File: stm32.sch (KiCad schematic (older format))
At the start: 30 parts, among them U3 STM32F205RBTx, U4 OLED_0.96\"_SSD1306, Y2 Crystal_GND24

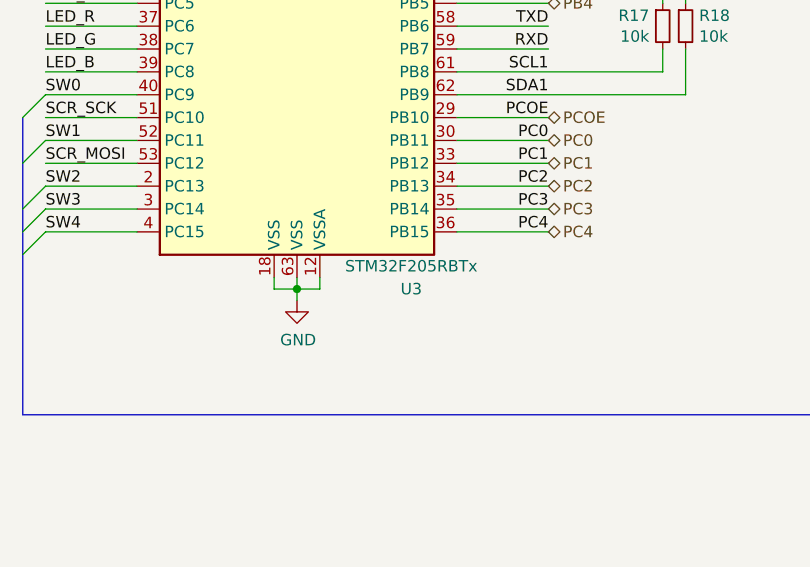
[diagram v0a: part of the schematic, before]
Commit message: sch, pcb: Replace STM32F205 with STM32F405
A Rust HAL is available for the F4 series and not for the F2 series...
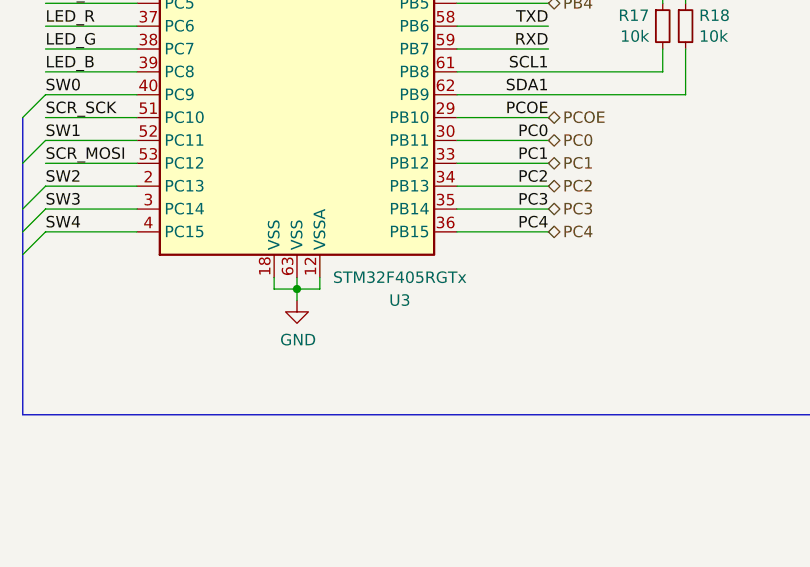
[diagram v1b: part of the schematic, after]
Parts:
- removed U3: STM32F205RBTx, Package_QFP:LQFP-64_10x10mm_P0.5mm, symbol MCU_ST_STM32F2:STM32F205RBTx
- added U3: STM32F405RGTx, Package_QFP:LQFP-64_10x10mm_P0.5mm, symbol MCU_ST_STM32F4:STM32F405RGTx
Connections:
- net +3V3: now also U3.1 (VBAT), U3.13 (VDDA), U3.19 (VDD), U3.32 (VDD), U3.48 (VDD), U3.64 (VDD)
- net DRDY: now also U3.50 (PA15)
- net GND: now also U3.12 (VSSA), U3.18 (VSS), U3.63 (VSS)
- net LED_A0: now also U3.54 (PD2)
- net LED_A1: now also U3.8 (PC0)
- net LED_A2: now also U3.9 (PC1)
- net LED_A3: now also U3.10 (PC2)
- net LED_A4: now also U3.11 (PC3)
- net LED_B: now also U3.39 (PC8)
- net LED_G: now also U3.38 (PC7)
- net LED_R: now also U3.37 (PC6)
- net PA0: now also U3.15 (PA1)
- net PA1: now also U3.16 (PA2)
- net PA2: now also U3.17 (PA3)
- net PA3: now also U3.20 (PA4)
- net PA4: now also U3.21 (PA5)
- net PA5: now also U3.22 (PA6)
- net PA6: now also U3.23 (PA7)
- net PA7: now also U3.41 (PA8)
- net PA8: now also U3.42 (PA9)
- net PA9: now also U3.43 (PA10)
- net PAOE: now also U3.14 (PA0)
- net PB0: now also U3.27 (PB1)
- net PB1: now also U3.28 (PB2)
- net PB2: now also U3.55 (PB3)
- net PB3: now also U3.56 (PB4)
- net PB4: now also U3.57 (PB5)
- net PBOE: now also U3.26 (PB0)
- net PC0: now also U3.30 (PB11)
- net PC1: now also U3.33 (PB12)
- net PC2: now also U3.34 (PB13)
- net PC3: now also U3.35 (PB14)
- net PC4: now also U3.36 (PB15)
- net PCOE: now also U3.29 (PB10)
- net RXD: now also U3.59 (PB7)
- net SCK_~CS: now also U3.25 (PC5)
- net SCL: now also U3.61 (PB8)
- net SCR_D~C: now also U3.24 (PC4)
- net SCR_MOSI: now also U3.53 (PC12)
- net SCR_SCK: now also U3.51 (PC10)
- net SDA: now also U3.62 (PB9)
- net SW0: now also U3.40 (PC9)
- net SW1: now also U3.52 (PC11)
- net SW2: now also U3.2 (PC13)
- net SW3: now also U3.3 (PC14)
- net SW4: now also U3.4 (PC15)
- net SWCLK: now also U3.49 (PA14)
- net SWDIO: now also U3.46 (PA13)
- net SWRST: now also U3.7 (NRST)
- net TXD: now also U3.58 (PB6)
- net USB_N: now also U3.44 (PA11)
- net USB_P: now also U3.45 (PA12)
- net at C19.1, Y2.1: now also U3.5 (PH0)
- net at C20.1, Y2.3: now also U3.6 (PH1)
- net at R12.2: now also U3.60 (BOOT0)
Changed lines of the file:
@@
 $EndDescr
-$Comp
-L MCU_ST_STM32F2:STM32F205RBTx U3
-U 1 1 5DFC281B
-P 5700 4050
-F 0 "U3" H 6200 2200 50  0000 C CNN
-F 1 "STM32F205RBTx" H 6200 2300 50  0000 C CNN
-F 2 "Package_QFP:LQFP-64_10x10mm_P0.5mm" H 5100 2350 50  0001 R CNN
-F 3 "http://www.st.com/st-web-ui/static/active/en/resource/technical/document/datasheet/CD00237391.pdf" H 5700 4050 50  0001 C CNN
-	1    5700 4050
-	1    0    0    -1
-$EndComp
 $Comp
 L power:+3V3 #PWR0124
@@
 Wire Wire Line
 	3900 3350 3900 3400
+Text Notes 5900 7550 0    50   ~ 0
+Red: 8mA@1.73V\nGreen: 5mA@2.7V\nBlue: 3mA@2.49V
 Wire Bus Line
 	4400 4050 4400 6450
@@
 Wire Bus Line
 	8300 5250 8300 6450
-Text Notes 5900 7550 0    50   ~ 0
-Red: 8mA@1.73V\nGreen: 5mA@2.7V\nBlue: 3mA@2.49V
+$Comp
+L MCU_ST_STM32F4:STM32F405RGTx U3
+U 1 1 5EFAF3AD
+P 5700 4050
+F 0 "U3" H 6150 2150 50  0000 C CNN
+F 1 "STM32F405RGTx" H 6150 2250 50  0000 C CNN
+F 2 "Package_QFP:LQFP-64_10x10mm_P0.5mm" H 5100 2350 50  0001 R CNN
+F 3 "http://www.st.com/st-web-ui/static/active/en/resource/technical/document/datasheet/DM00037051.pdf" H 5700 4050 50  0001 C CNN
+	1    5700 4050
+	1    0    0    -1
+$EndComp
 $EndSCHEMATC

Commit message: sch: List LCSC P/N for each component
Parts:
- C12, C13, C14, C15, C16, C17, C18, C19, C20, C21: LCSC P/N (none) -> C1591; MFR P/N (none) -> CL10B104KB8NNNC
- D3, D4, D5, D6, D7: LCSC P/N (none) -> C404281; MFR P/N (none) -> MHPA1515RGBDT
- R11, R13: LCSC P/N (none) -> C327826; MFR P/N (none) -> MR06X1003FTL
- R12, R17, R18: LCSC P/N (none) -> C115324; MFR P/N (none) -> RS-03K1002FT
- R14: LCSC P/N (none) -> C429538; MFR P/N (none) -> CR0603F196RP05
- R15: LCSC P/N (none) -> C22787; MFR P/N (none) -> 0603WAF1200T5E
- R16: LCSC P/N (none) -> C286581; MFR P/N (none) -> RS-03K2700FT
- S1: LCSC P/N (none) -> C145899; MFR P/N (none) -> K1-5202UA-03
- U3: LCSC P/N (none) -> C15742; MFR P/N (none) -> STM32F405RGT6
- U4: LCSC P/N (none) -> C358721; MFR P/N (none) -> MTF185-107SY1
- Y2: LCSC P/N (none) -> C400090; MFR P/N (none) -> TAXM8M4RDBCCT2T
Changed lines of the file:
@@
 F 2 "Resistor_SMD:R_0603_1608Metric" H 4400 2300 50  0001 C CNN
 F 3 "~" H 4400 2300 50  0001 C CNN
+F 4 "C327826" H 4400 2300 50  0001 C CNN "LCSC P/N"
+F 5 "MR06X1003FTL" H 4400 2300 50  0001 C CNN "MFR P/N"
 	1    4400 2300
 	1    0    0    -1
@@
 F 2 "Capacitor_SMD:C_0603_1608Metric" H 4400 2600 50  0001 C CNN
 F 3 "~" H 4400 2600 50  0001 C CNN
+F 4 "C1591" H 4400 2600 50  0001 C CNN "LCSC P/N"
+F 5 "CL10B104KB8NNNC" H 4400 2600 50  0001 C CNN "MFR P/N"
 	1    4400 2600
 	1    0    0    1
@@
 F 2 "Resistor_SMD:R_0603_1608Metric" H 4800 2650 50  0001 C CNN
 F 3 "~" H 4800 2650 50  0001 C CNN
+F 4 "C115324" H 4800 2650 50  0001 C CNN "LCSC P/N"
+F 5 "RS-03K1002FT" H 4800 2650 50  0001 C CNN "MFR P/N"
 	1    4800 2650
 	0    -1   1    0
@@
 F 2 "Capacitor_SMD:C_0603_1608Metric" H 4750 1300 50  0001 C CNN
 F 3 "~" H 4750 1300 50  0001 C CNN
+F 4 "C1591" H 4750 1300 50  0001 C CNN "LCSC P/N"
+F 5 "CL10B104KB8NNNC" H 4750 1300 50  0001 C CNN "MFR P/N"
 	1    4750 1300
 	-1   0    0    -1
@@
 F 2 "Capacitor_SMD:C_0603_1608Metric" H 5150 1300 50  0001 C CNN
 F 3 "~" H 5150 1300 50  0001 C CNN
+F 4 "C1591" H 5150 1300 50  0001 C CNN "LCSC P/N"
+F 5 "CL10B104KB8NNNC" H 5150 1300 50  0001 C CNN "MFR P/N"
 	1    5150 1300
 	-1   0    0    -1
@@
 F 2 "Capacitor_SMD:C_0603_1608Metric" H 5550 1300 50  0001 C CNN
 F 3 "~" H 5550 1300 50  0001 C CNN
+F 4 "C1591" H 5550 1300 50  0001 C CNN "LCSC P/N"
+F 5 "CL10B104KB8NNNC" H 5550 1300 50  0001 C CNN "MFR P/N"
 	1    5550 1300
 	-1   0    0    -1
@@
 F 2 "Capacitor_SMD:C_0603_1608Metric" H 5950 1300 50  0001 C CNN
 F 3 "~" H 5950 1300 50  0001 C CNN
+F 4 "C1591" H 5950 1300 50  0001 C CNN "LCSC P/N"
+F 5 "CL10B104KB8NNNC" H 5950 1300 50  0001 C CNN "MFR P/N"
 	1    5950 1300
 	-1   0    0    -1
@@
 F 2 "Capacitor_SMD:C_0603_1608Metric" H 6350 1300 50  0001 C CNN
 F 3 "~" H 6350 1300 50  0001 C CNN
+F 4 "C1591" H 6350 1300 50  0001 C CNN "LCSC P/N"
+F 5 "CL10B104KB8NNNC" H 6350 1300 50  0001 C CNN "MFR P/N"
 	1    6350 1300
 	-1   0    0    -1
@@
 F 2 "Capacitor_SMD:C_0603_1608Metric" H 6750 1300 50  0001 C CNN
 F 3 "~" H 6750 1300 50  0001 C CNN
+F 4 "C1591" H 6750 1300 50  0001 C CNN "LCSC P/N"
+F 5 "CL10B104KB8NNNC" H 6750 1300 50  0001 C CNN "MFR P/N"
 	1    6750 1300
 	-1   0    0    -1
@@
 F 2 "Resistor_SMD:R_0603_1608Metric" H 7300 4750 50  0001 C CNN
 F 3 "~" H 7300 4750 50  0001 C CNN
+F 4 "C115324" H 7300 4750 50  0001 C CNN "LCSC P/N"
+F 5 "RS-03K1002FT" H 7300 4750 50  0001 C CNN "MFR P/N"
 	1    7300 4750
 	1    0    0    -1
@@
 F 2 "Resistor_SMD:R_0603_1608Metric" H 7400 4750 50  0001 C CNN
 F 3 "~" H 7400 4750 50  0001 C CNN
+F 4 "C115324" H 7400 4750 50  0001 C CNN "LCSC P/N"
+F 5 "RS-03K1002FT" H 7400 4750 50  0001 C CNN "MFR P/N"
 	1    7400 4750
 	1    0    0    -1
@@
 F 2 "antboard:K1-5202UA-03" H 8900 5050 50  0001 C CNN
 F 3 "https://datasheet.lcsc.com/szlcsc/1809211421_Korean-Hroparts-Elec-K1-5202UA-03_C145899.pdf" H 8900 5050 50  0001 C CNN
+F 4 "C145899" H 8900 5050 50  0001 C CNN "LCSC P/N"
+F 5 "K1-5202UA-03" H 8900 5050 50  0001 C CNN "MFR P/N"
 	1    8900 5050
 	1    0    0    -1
@@
 F 2 "Resistor_SMD:R_0603_1608Metric" H 5250 7350 50  0001 C CNN
 F 3 "~" H 5250 7350 50  0001 C CNN
+F 4 "C429538" H 5250 7350 50  0001 C CNN "LCSC P/N"
+F 5 "CR0603F196RP05" H 5250 7350 50  0001 C CNN "MFR P/N"
 	1    5250 7350
 	0    -1   1    0
@@
 F 2 "Resistor_SMD:R_0603_1608Metric" H 5250 7450 50  0001 C CNN
 F 3 "~" H 5250 7450 50  0001 C CNN
+F 4 "C22787" H 5250 7450 50  0001 C CNN "LCSC P/N"
+F 5 "0603WAF1200T5E" H 5250 7450 50  0001 C CNN "MFR P/N"
 	1    5250 7450
 	0    -1   1    0
@@
 F 2 "Resistor_SMD:R_0603_1608Metric" H 5250 7550 50  0001 C CNN
 F 3 "~" H 5250 7550 50  0001 C CNN
+F 4 "C286581" H 5250 7550 50  0001 C CNN "LCSC P/N"
+F 5 "RS-03K2700FT" H 5250 7550 50  0001 C CNN "MFR P/N"
 	1    5250 7550
 	0    -1   1    0
@@
 F 2 "antboard:OLED_0.96_SSD1306" H 1300 4700 50  0001 C CNN
 F 3 "https://datasheet.lcsc.com/szlcsc/1809201020_Jixin-JX04010101_C131691.pdf" H 1300 4700 50  0001 C CNN
+F 4 "C358721" H 2150 4700 50  0001 C CNN "LCSC P/N"
+F 5 "MTF185-107SY1" H 2150 4700 50  0001 C CNN "MFR P/N"
 	1    2150 4700
 	-1   0    0    -1
@@
 F 2 "Capacitor_SMD:C_0603_1608Metric" H 2800 5250 50  0001 C CNN
 F 3 "~" H 2800 5250 50  0001 C CNN
+F 4 "C1591" H 2800 5250 50  0001 C CNN "LCSC P/N"
+F 5 "CL10B104KB8NNNC" H 2800 5250 50  0001 C CNN "MFR P/N"
 	1    2800 5250
 	-1   0    0    1
@@
 F 2 "Resistor_SMD:R_0603_1608Metric" H 2800 4750 50  0001 C CNN
 F 3 "~" H 2800 4750 50  0001 C CNN
+F 4 "C327826" H 2800 4750 50  0001 C CNN "LCSC P/N"
+F 5 "MR06X1003FTL" H 2800 4750 50  0001 C CNN "MFR P/N"
 	1    2800 4750
 	1    0    0    -1
@@
 F 2 "antboard:PLCC1515" H 1000 7000 50  0001 C CNN
 F 3 "~" H 1000 7000 50  0001 C CNN
+F 4 "C404281" H 1000 7050 50  0001 C CNN "LCSC P/N"
+F 5 "MHPA1515RGBDT" H 1000 7050 50  0001 C CNN "MFR P/N"
 	1    1000 7050
 	0    -1   -1   0
@@
 F 2 "antboard:PLCC1515" H 1750 7000 50  0001 C CNN
 F 3 "~" H 1750 7000 50  0001 C CNN
+F 4 "C404281" H 1750 7050 50  0001 C CNN "LCSC P/N"
+F 5 "MHPA1515RGBDT" H 1750 7050 50  0001 C CNN "MFR P/N"
 	1    1750 7050
 	0    -1   -1   0
@@
 F 2 "antboard:PLCC1515" H 2500 7000 50  0001 C CNN
 F 3 "~" H 2500 7000 50  0001 C CNN
+F 4 "C404281" H 2500 7050 50  0001 C CNN "LCSC P/N"
+F 5 "MHPA1515RGBDT" H 2500 7050 50  0001 C CNN "MFR P/N"
 	1    2500 7050
 	0    -1   -1   0
@@
 F 2 "antboard:PLCC1515" H 3250 7000 50  0001 C CNN
 F 3 "~" H 3250 7000 50  0001 C CNN
+F 4 "C404281" H 3250 7050 50  0001 C CNN "LCSC P/N"
+F 5 "MHPA1515RGBDT" H 3250 7050 50  0001 C CNN "MFR P/N"
 	1    3250 7050
 	0    -1   -1   0
@@
 F 2 "antboard:PLCC1515" H 4000 7000 50  0001 C CNN
 F 3 "~" H 4000 7000 50  0001 C CNN
+F 4 "C404281" H 4000 7050 50  0001 C CNN "LCSC P/N"
+F 5 "MHPA1515RGBDT" H 4000 7050 50  0001 C CNN "MFR P/N"
 	1    4000 7050
 	0    -1   -1   0
@@
 F 2 "Capacitor_SMD:C_0603_1608Metric" H 4050 4150 50  0001 C CNN
 F 3 "~" H 4050 4150 50  0001 C CNN
+F 4 "C1591" H 4050 4150 50  0001 C CNN "LCSC P/N"
+F 5 "CL10B104KB8NNNC" H 4050 4150 50  0001 C CNN "MFR P/N"
 	1    4050 4150
 	-1   0    0    -1
@@
 F 2 "Capacitor_SMD:C_0603_1608Metric" H 3550 4150 50  0001 C CNN
 F 3 "~" H 3550 4150 50  0001 C CNN
+F 4 "C1591" H 3550 4150 50  0001 C CNN "LCSC P/N"
+F 5 "CL10B104KB8NNNC" H 3550 4150 50  0001 C CNN "MFR P/N"
 	1    3550 4150
 	-1   0    0    -1
@@
 F 2 "Crystal:Crystal_SMD_3225-4Pin_3.2x2.5mm" H 3800 3950 50  0001 C CNN
 F 3 "~" H 3800 3950 50  0001 C CNN
+F 4 "C400090" H 3800 3950 50  0001 C CNN "LCSC P/N"
+F 5 "TAXM8M4RDBCCT2T" H 3800 3950 50  0001 C CNN "MFR P/N"
 	1    3800 3950
 	1    0    0    -1
@@
 F 2 "Package_QFP:LQFP-64_10x10mm_P0.5mm" H 5100 2350 50  0001 R CNN
 F 3 "http://www.st.com/st-web-ui/static/active/en/resource/technical/document/datasheet/DM00037051.pdf" H 5700 4050 50  0001 C CNN
+F 4 "C15742" H 5700 4050 50  0001 C CNN "LCSC P/N"
+F 5 "STM32F405RGT6" H 5700 4050 50  0001 C CNN "MFR P/N"
 	1    5700 4050
 	1    0    0    -1

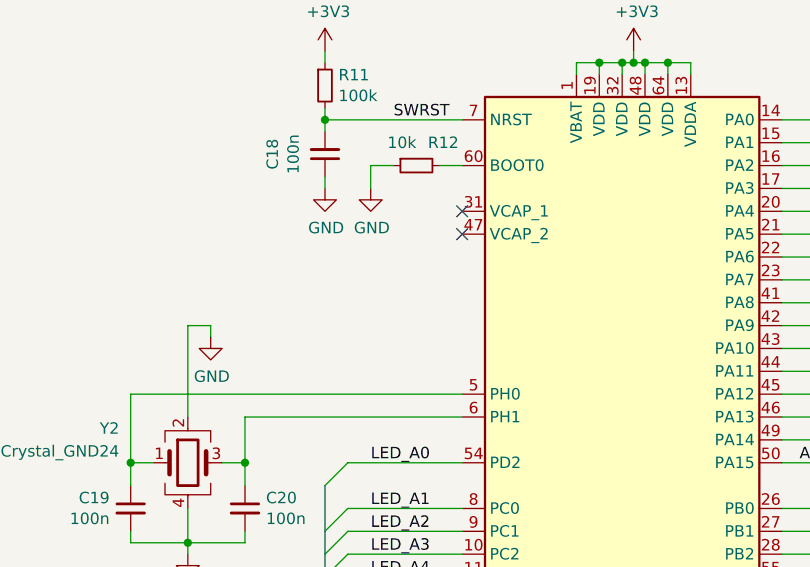
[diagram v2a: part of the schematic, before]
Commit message: *: Add VCAP decoupling caps
CPU had strange behaviours without it (IRQs fired only once, random
SEGFAULTs, ...)
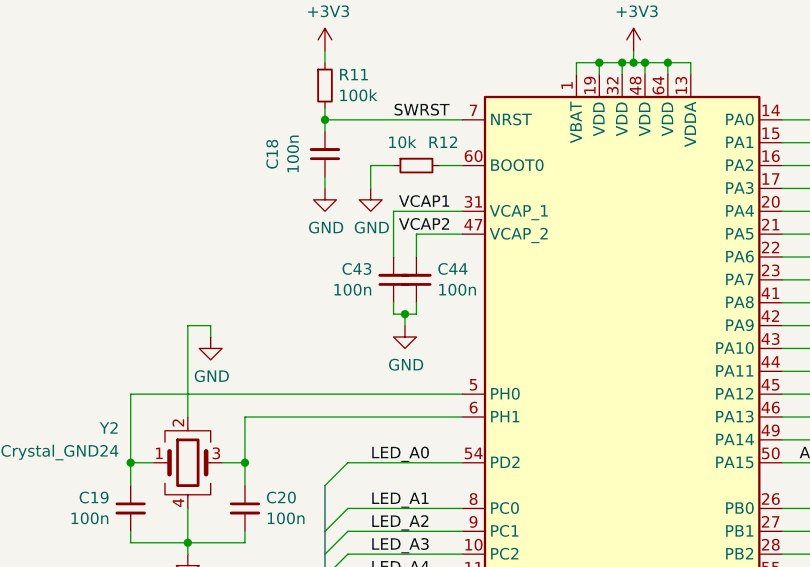
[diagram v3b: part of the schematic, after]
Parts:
- added C43, C44: 100n, Capacitor_SMD:C_0603_1608Metric, symbol Device:C_Small
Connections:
- net GND: now also C43.1, C44.1
- net VCAP1: now reaches U3.31 (VCAP_1)
- net VCAP1: now also C43.2
- net VCAP2: now reaches U3.47 (VCAP_2)
- net VCAP2: now also C44.2
- no-connect marks 2 -> 0

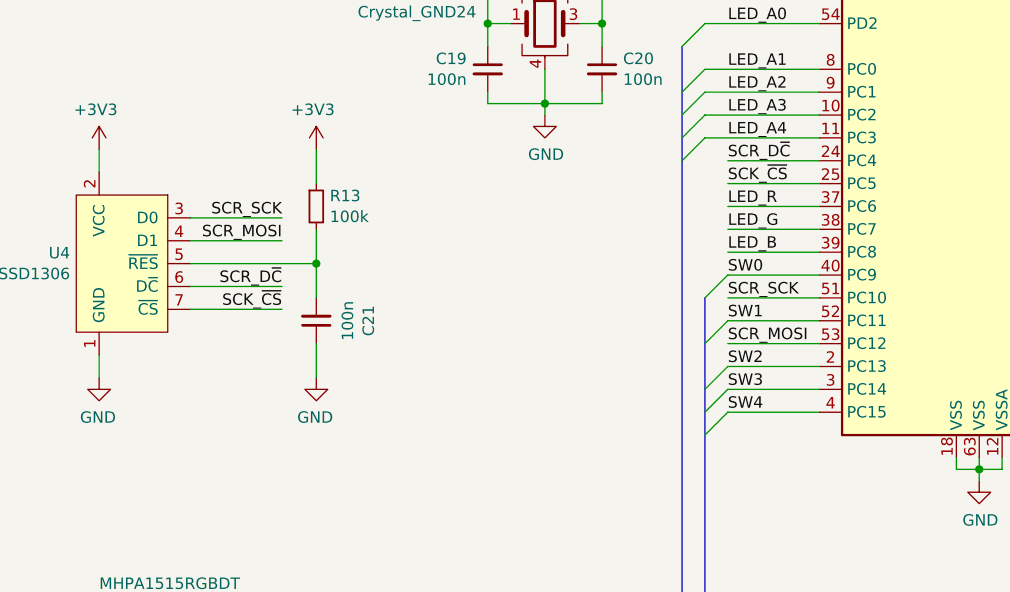
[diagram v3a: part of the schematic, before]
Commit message: sch, pcb: Repurpose OLED CS as OLED RST
Since the OLED is the only device off the SPI bus, it makes no sense to
have a CS pin
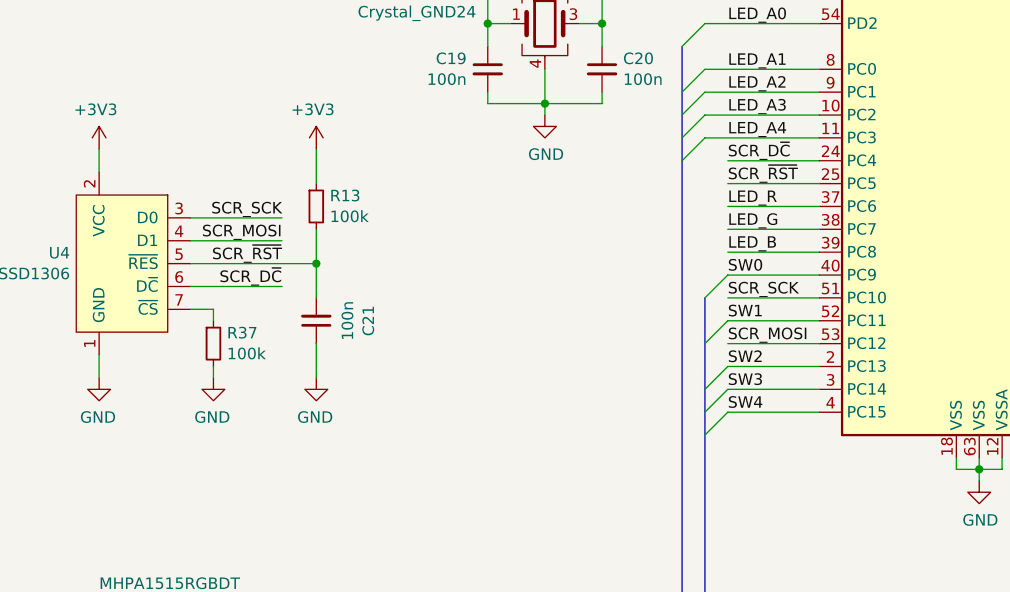
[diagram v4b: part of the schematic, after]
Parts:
- added R37: 100k, Resistor_SMD:R_0603_1608Metric, symbol Device:R_Small
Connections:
- net GND: now also R37.2
- net SCR_~RST: now reaches C21.2, R13.2, U4.5 (~RES)
- net SCR_~RST: now also U3.25 (PC5)
- net SCK_~CS: no longer names the net of U4.7 (~CS)
- net SCK_~CS: now also R37.1; no longer U3.25 (PC5)
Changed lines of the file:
@@
 Text Label 4600 4550 0    50   ~ 0
 SCR_D~C
-Text Label 4600 4650 0    50   ~ 0
-SCK_~CS
 Wire Wire Line
 	5350 7350 5750 7350
@@
 Text Label 4950 2850 2    50   ~ 0
 VCAP1
-Wire Wire Line
-	2800 5350 2800 5500
+Text Label 4950 2950 2    50   ~ 0
+VCAP2
 $Comp
 L power:GND #PWR?
@@
 	-1   0    0    -1
 $EndComp
-Wire Wire Line
-	1850 5400 1850 5500
 $Comp
 L power:GND #PWR?
@@
 	-1   0    0    -1
 $EndComp
-Text Label 2650 5200 2    50   ~ 0
-SCK_~CS
-Wire Wire Line
-	2250 5200 2650 5200
+Wire Wire Line
+	2800 5350 2800 5500
+Wire Wire Line
+	1850 5400 1850 5500
+$Comp
+L Device:R_Small R?
+U 1 1 5F0C692E
+P 2350 5350
+AR Path="/5DF7E971/5F0C692E" Ref="R?"  Part="1"
+AR Path="/5DFC2583/5F0C692E" Ref="R37"  Part="1"
+F 0 "R37" H 2409 5396 50  0000 L CNN
+F 1 "100k" H 2409 5305 50  0000 L CNN
+F 2 "Resistor_SMD:R_0603_1608Metric" H 2350 5350 50  0001 C CNN
+F 3 "~" H 2350 5350 50  0001 C CNN
+F 4 "C327826" H 2350 5350 50  0001 C CNN "LCSC P/N"
+F 5 "MR06X1003FTL" H 2350 5350 50  0001 C CNN "MFR P/N"
+	1    2350 5350
+	1    0    0    -1
+$EndComp
+$Comp
+L power:GND #PWR?
+U 1 1 5F0C716A
+P 2350 5500
+AR Path="/5F0C716A" Ref="#PWR?"  Part="1"
+AR Path="/5DF7E971/5F0C716A" Ref="#PWR?"  Part="1"
+AR Path="/5DFC2583/5F0C716A" Ref="#PWR064"  Part="1"
+F 0 "#PWR064" H 2350 5250 50  0001 C CNN
+F 1 "GND" H 2355 5327 50  0000 C CNN
+F 2 "" H 2350 5500 50  0001 C CNN
+F 3 "" H 2350 5500 50  0001 C CNN
+	1    2350 5500
+	-1   0    0    -1
+$EndComp
+Wire Wire Line
+	2250 5200 2350 5200
+Wire Wire Line
+	2350 5200 2350 5250
+Wire Wire Line
+	2350 5450 2350 5500
+Text Label 2650 5000 2    50   ~ 0
+SCR_~RST
+Text Label 4600 4650 0    50   ~ 0
+SCR_~RST
 Wire Bus Line
 	4400 4050 4400 6450
-Wire Bus Line
-	8300 5250 8300 6450
 Wire Bus Line
 	1100 6450 4400 6450
 Wire Bus Line
 	4500 5150 4500 6450
-Text Label 4950 2950 2    50   ~ 0
-VCAP2
+Wire Bus Line
+	8300 5250 8300 6450
 $EndSCHEMATC
